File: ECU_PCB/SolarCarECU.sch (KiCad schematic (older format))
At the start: 176 parts, among them J2 Screw_Terminal_01x08, J3 Screw_Terminal_01x08, J4 Screw_Terminal_01x08, J5 Screw_Terminal_01x08, J6 Screw_Terminal_01x08, J7 Screw_Terminal_01x08, J8 Screw_Terminal_01x08, Q1 QM6015D, Q2 QM6015D, Q3 QM6015D, Q4 QM6015D, Q5 QM6015D, Q6 QM6015D, Q7 QM6015D, U1 Teensy3.6, U10 LM324A, U11 MCP1403, U2 MCP1403, U3 MCP1403, U4 L7805, U5 MCP2562-E-P, U6 MCP2562-E-P, U7 4504, U8 4504, U9 4504

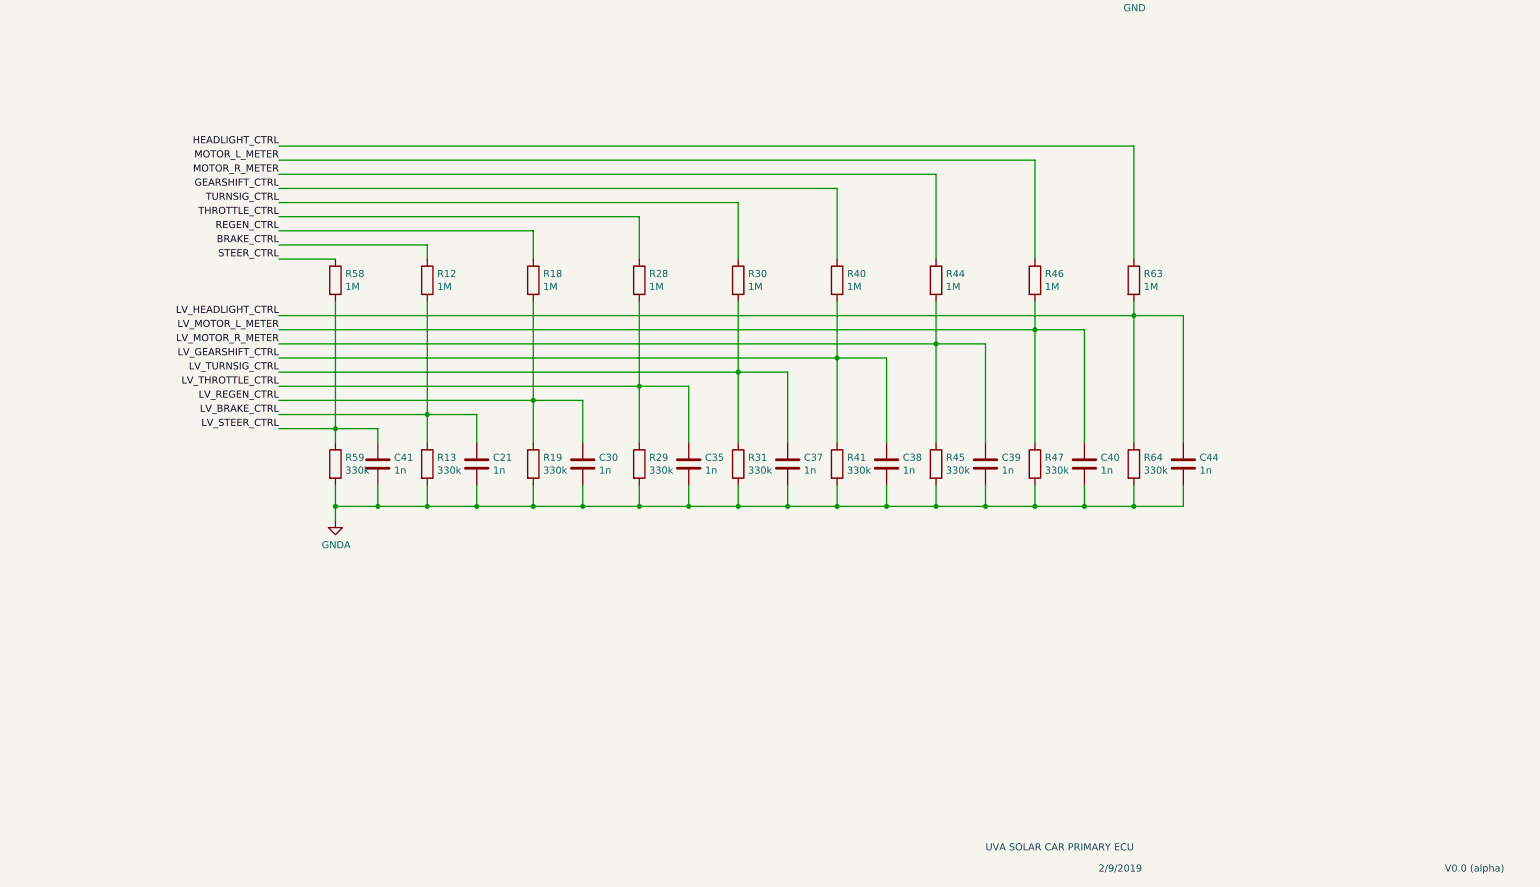
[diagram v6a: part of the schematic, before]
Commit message: added resistors to handle floating  condition
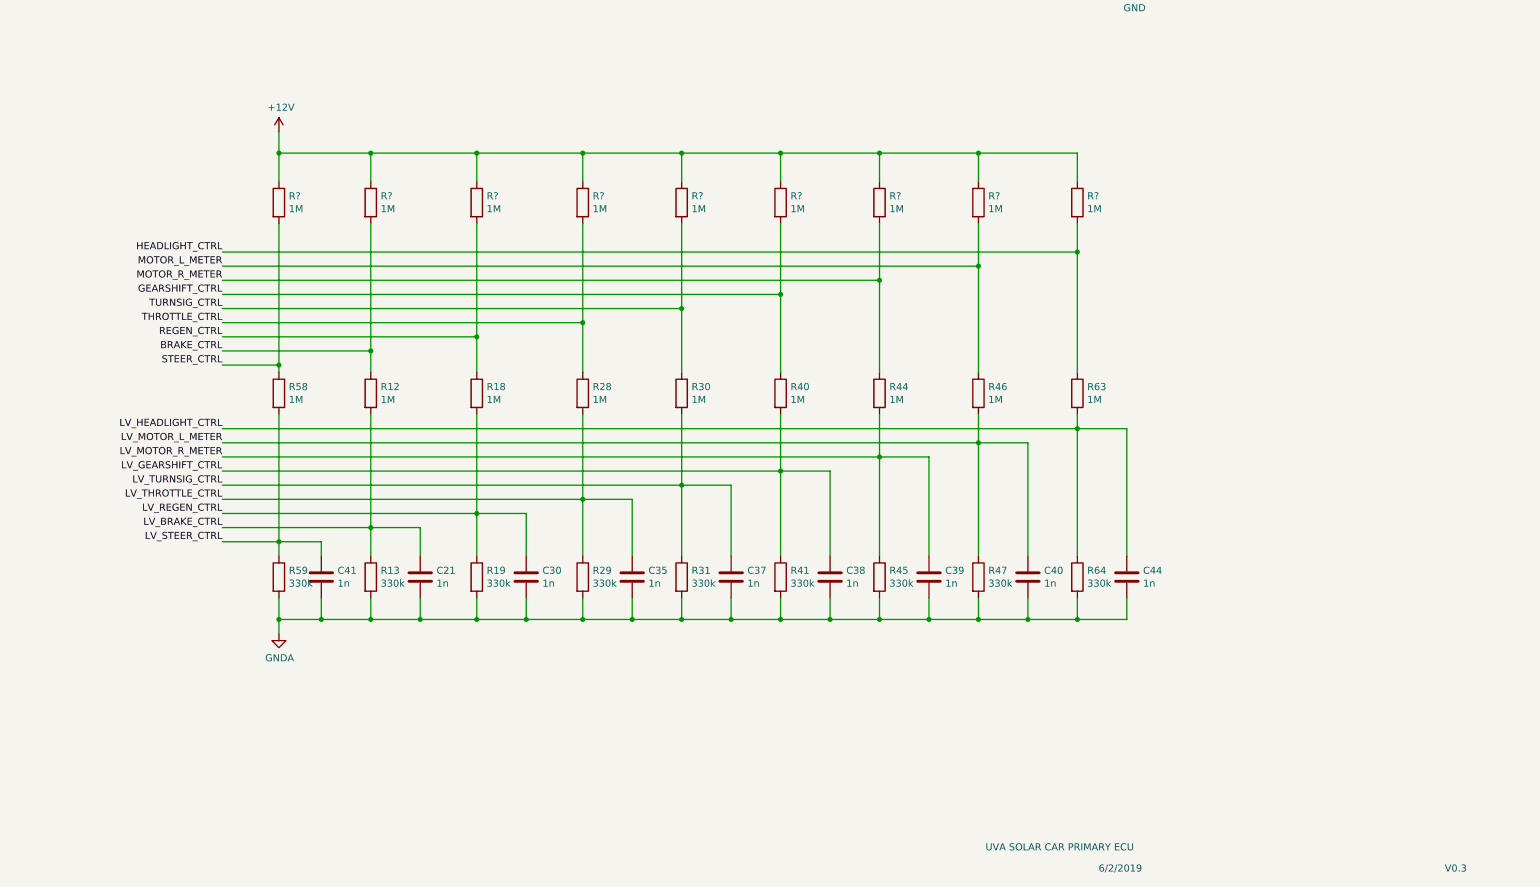
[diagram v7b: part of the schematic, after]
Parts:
- added R? (x9): 1M, Resistor_SMD:R_0603_1608Metric, symbol SolarCarECU-rescue:R-Device-SolarCarECU-rescue
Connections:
- net +12V: now also R?.1, R?.1, R?.1, R?.1, R?.1, R?.1, R?.1, R?.1, R?.1
- net BRAKE_CTRL: now also R?.2
- net GEARSHIFT_CTRL: now also R?.2
- net HEADLIGHT_CTRL: now also R?.2
- net MOTOR_L_METER: now also R?.2
- net MOTOR_R_METER: now also R?.2
- net REGEN_CTRL: now also R?.2
- net STEER_CTRL: now also R?.2
- net THROTTLE_CTRL: now also R?.2
- net TURNSIG_CTRL: now also R?.2
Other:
- note added: "6/2/2019"
- note added: "V0.3"
- note removed: "2/9/2019\n"
- note removed: "V0.0 (alpha)"
- moved on the sheet: C21, C30, C35, C37, C38, C39, C40, C41, C44, R12, R13, R18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

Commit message: finished PCB
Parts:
- removed R1, R2, R3, R4: 0, Resistor_SMD:R_1206_3216Metric, symbol SolarCarECU-rescue:R-Device-SolarCarECU-rescue
- renumbered C15 to C?, C13 to C?, C16 to C?, C14 to C?, C39 to C?, C40 to C?, C44 to C?, C42 to C?, C19 to C?, C41 to C?, C21 to C?, C30 to C?, C35 to C?, C37 to C?, C38 to C?, C18 to C?, C17 to C?, C20 to C?, C36 to C?, D16 to D?, R8 to R?, R10 to R?, R11 to R?, R9 to R?, R45 to R?, R44 to R?, R47 to R?, R46 to R?, R48 to R?, R49 to R?, R50 to R?, R51 to R?, R7 to R?, R43 to R?, R63 to R?, R64 to R?, R60 to R?, R58 to R?, R53 to R?, R52 to R?, R59 to R?, R5 to R?, R42 to R?, R54 to R?, R55 to R?, R56 to R?, R57 to R?, R13 to R?, R19 to R?, R29 to R?, R31 to R?, R12 to R?, R18 to R?, R28 to R?, R41 to R?, R40 to R?, R61 to R?, R62 to R?, R6 to R?
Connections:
- net CAN0_RX: now also U1.22 (30_PWM_can0rx_Touch)
- net CAN0_TX: now also U1.21 (29_PWM_can0tx_Touch)
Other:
- moved on the sheet: R?
